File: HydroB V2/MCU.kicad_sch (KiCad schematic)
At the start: 9 parts, among them U1 ESP32-S3-WROOM-1-N16R2

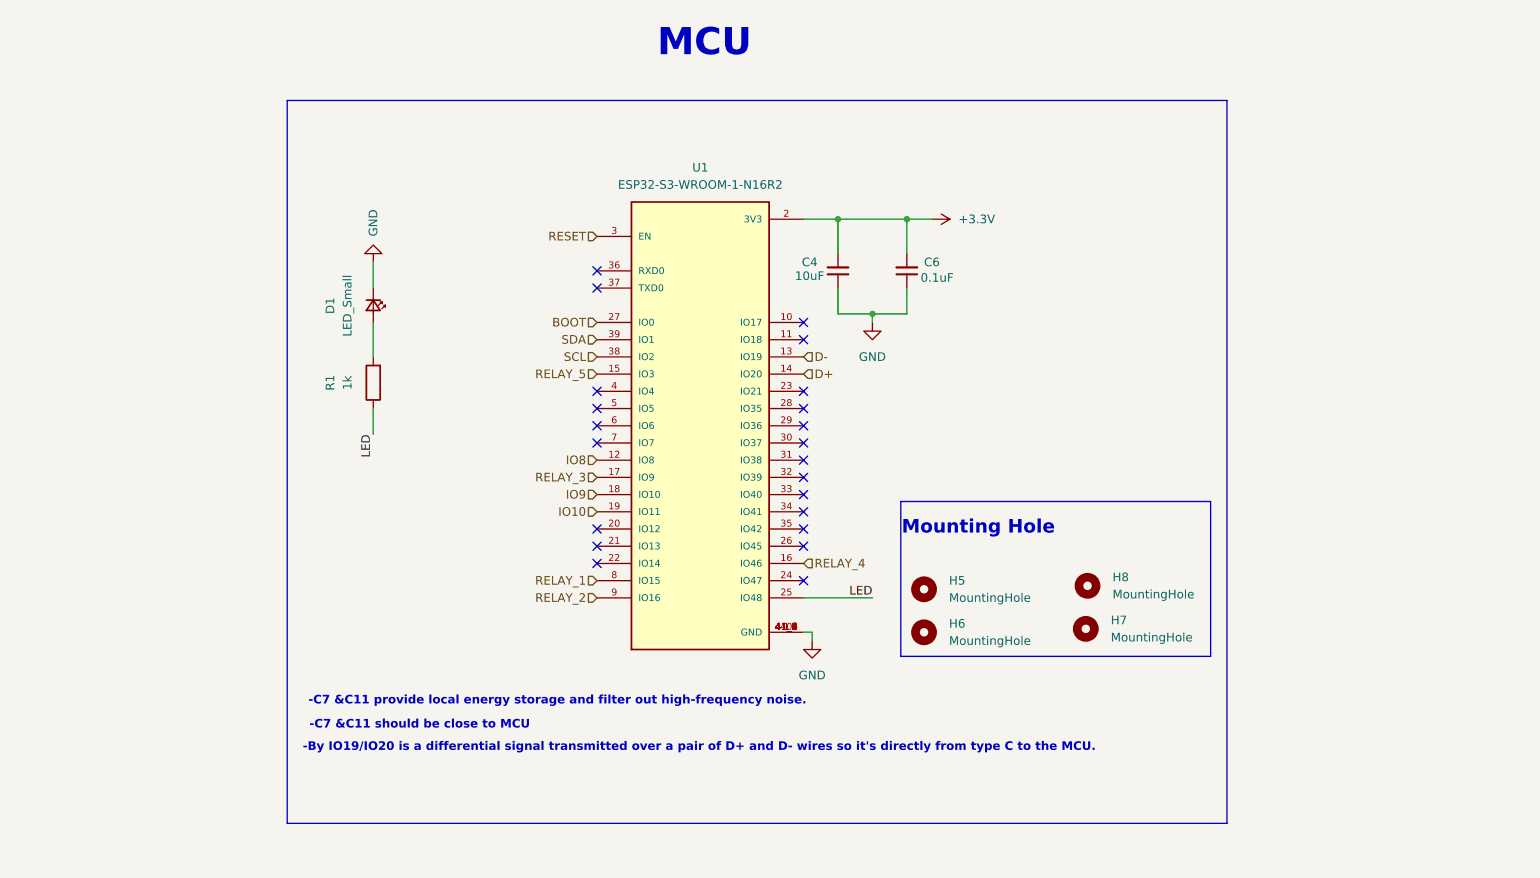
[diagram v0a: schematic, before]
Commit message: Update power supply and connector of sensor
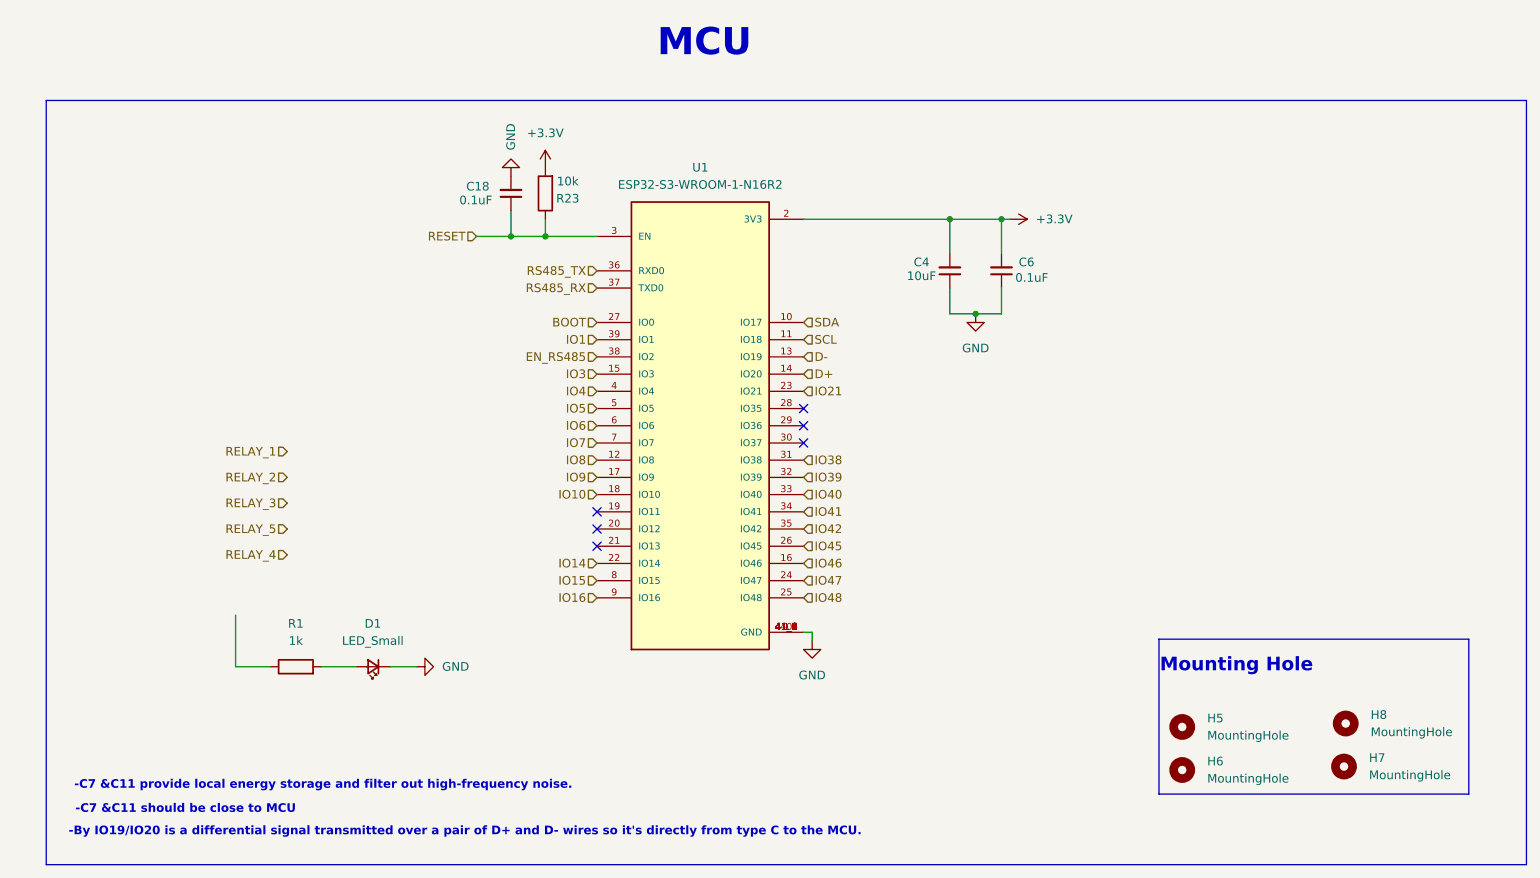
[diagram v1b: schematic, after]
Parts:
- added C18: 0.1uF, Capacitor_SMD:C_0603_1608Metric, symbol Device:C_Small
- added R23: 10k, Resistor_SMD:R_0603_1608Metric, symbol Device:R
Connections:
- net +3.3V: now also R23.2
- net GND: now also C18.2
- net IO10: now also U1.18 (IO10); no longer U1.19 (IO11)
- net IO9: now also U1.17 (IO9); no longer U1.18 (IO10)
- net RELAY_1: no longer U1.8 (IO15)
- net RELAY_2: no longer U1.9 (IO16)
- net RELAY_3: no longer U1.17 (IO9)
- net RELAY_4: no longer U1.16 (IO46)
- net RELAY_5: no longer U1.15 (IO3)
- net RESET: now also C18.1, R23.1
- net SCL: now also U1.11 (IO18); no longer U1.38 (IO2)
- net SDA: now also U1.10 (IO17); no longer U1.39 (IO1)
- net IO14: now reaches U1.22 (IO14)
- net IO21: now reaches U1.23 (IO21)
- net IO47: now reaches U1.24 (IO47)
- net IO45: now reaches U1.26 (IO45)
- net IO38: now reaches U1.31 (IO38)
- net IO39: now reaches U1.32 (IO39)
- net IO40: now reaches U1.33 (IO40)
- net IO41: now reaches U1.34 (IO41)
- net IO42: now reaches U1.35 (IO42)
- net RS485_TX: now reaches U1.36 (RXD0)
- net RS485_RX: now reaches U1.37 (TXD0)
- net IO4: now reaches U1.4 (IO4)
- net IO5: now reaches U1.5 (IO5)
- net IO6: now reaches U1.6 (IO6)
- net IO7: now reaches U1.7 (IO7)
- net LED: no longer names the net of R1.1
- net LED: no longer U1.25 (IO48)
- new net EN_RS485: U1.38 (IO2)
- new net IO1: U1.39 (IO1)
- new net IO15: U1.8 (IO15)
- new net IO16: U1.9 (IO16)
- new net IO3: U1.15 (IO3)
- new net IO46: U1.16 (IO46)
- new net IO48: U1.25 (IO48)
- no-connect marks 22 -> 6
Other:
- moved on the sheet: C4, C6, D1, H5, H6, H7, H8, R1
